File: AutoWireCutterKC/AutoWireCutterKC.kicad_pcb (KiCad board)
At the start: 2 copper layers, 35.8 x 41.7 mm, 20 parts, among them J1 LCD I/O, J2 ISP, J8 Barrel_Jack, J9 Stepper, M1 Conn_01x01_Male, M2 Conn_01x01_Male, M3 Conn_01x01_Male, U1 ATMEGA328P-AU, U2 MCP1700_SOT23, U3 LT1129-5.0_SOT223

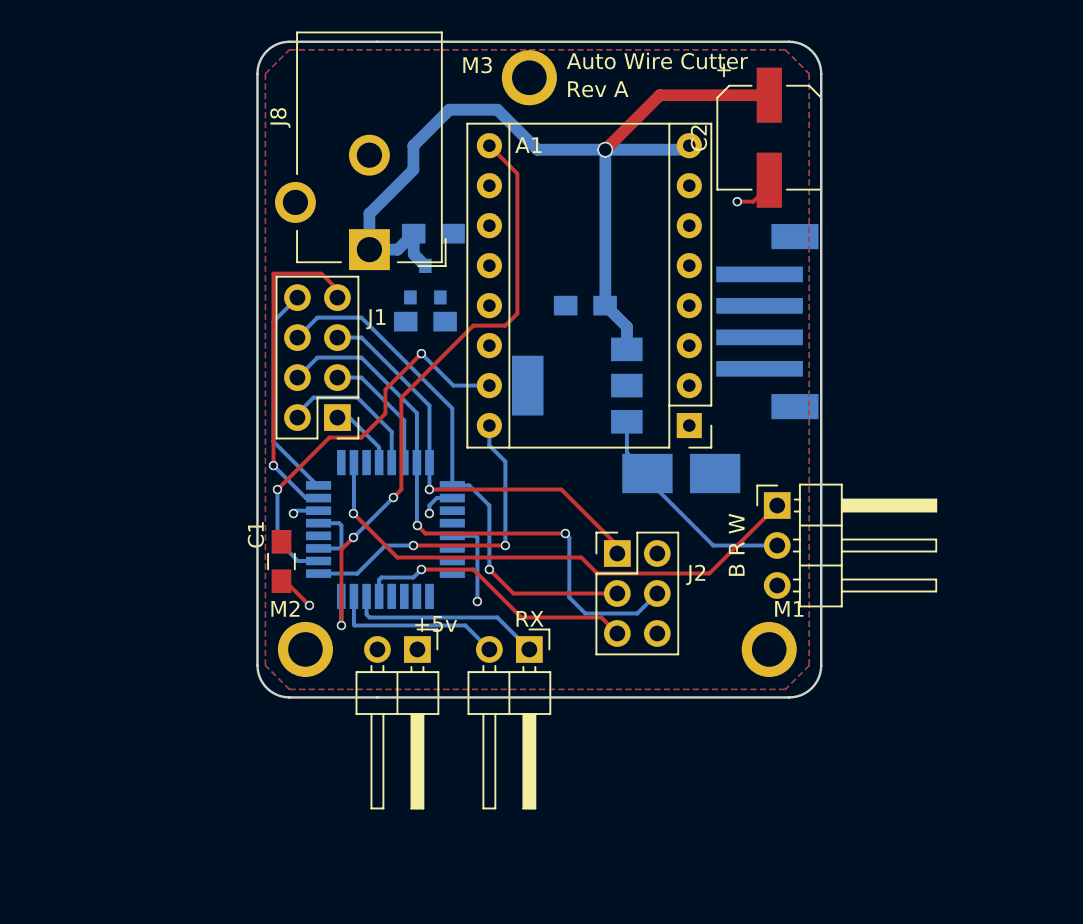
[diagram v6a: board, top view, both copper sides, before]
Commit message: Final Version
Board edge cuts need updating. Otherwise ready to order.
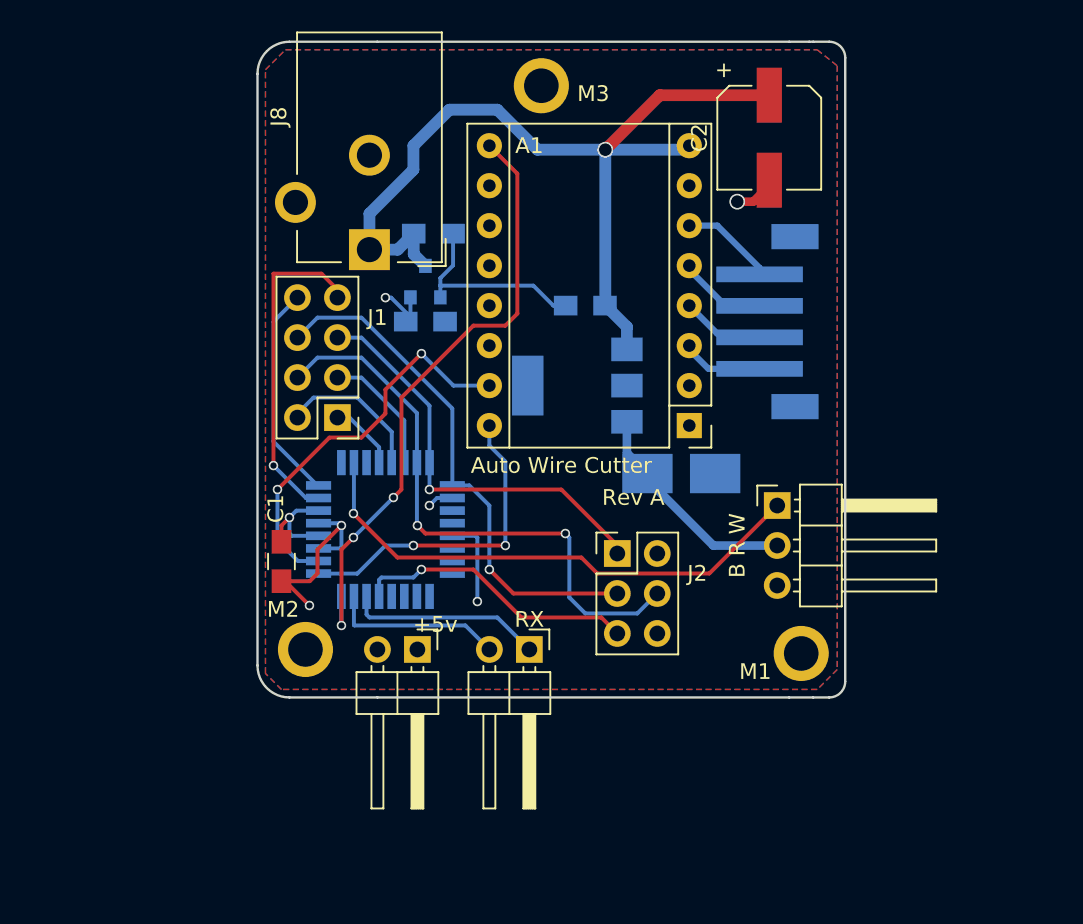
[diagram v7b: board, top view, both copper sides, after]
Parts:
- moved M1 2.05 mm to (169.2, 117.1)
- moved M3 0.92 mm to (152.7, 81.0)
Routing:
- net GND: track 15.3 -> 34.3 mm, vias 3 -> 4
- net +5VL: track 3.83 -> 11.7 mm, vias 2 -> 3
- net Net-(A1-Pad6): track 0.00 -> 5.99 mm
- net Net-(A1-Pad5): track 0.00 -> 5.67 mm
- net Net-(A1-Pad4): track 0.00 -> 5.30 mm
- net Net-(A1-Pad3): track 0.00 -> 5.22 mm
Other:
- board size 35.8 x 41.7 mm -> 37.3 x 41.7 mm
- rule pad_to_mask_clearance: 0.2 -> 0.0508
